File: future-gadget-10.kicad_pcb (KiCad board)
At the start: 2 copper layers, 147.3 x 157.5 mm, 38 parts, among them J1 Conn_02x05_Odd_Even, U1 ProMicro

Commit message: Adds right hand, and updates the connector to be vertical to avoid orientation issues.
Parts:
- added D19: D_Small, Diode_SMD:D_SOD-123, B.Cu at (452.1, 129.5)
- added D20: D_Small, Diode_SMD:D_SOD-123, B.Cu at (431.8, 129.5)
- added D21: D_Small, Diode_SMD:D_SOD-123, B.Cu at (411.5, 119.4)
- added D22: D_Small, Diode_SMD:D_SOD-123, B.Cu at (391.2, 119.4)
- added D23: D_Small, Diode_SMD:D_SOD-123, B.Cu at (370.8, 129.5)
- added D24: D_Small, Diode_SMD:D_SOD-123, B.Cu at (452.1, 149.9)
- added D25: D_Small, Diode_SMD:D_SOD-123, B.Cu at (431.8, 149.9)
- added D26: D_Small, Diode_SMD:D_SOD-123, B.Cu at (411.5, 139.7)
- added D27: D_Small, Diode_SMD:D_SOD-123, B.Cu at (391.2, 139.7)
- added D28: D_Small, Diode_SMD:D_SOD-123, B.Cu at (370.8, 149.9)
- added D29: D_Small, Diode_SMD:D_SOD-123, B.Cu at (452.1, 170.2)
- added D30: D_Small, Diode_SMD:D_SOD-123, B.Cu at (431.8, 170.2)
- added D31: D_Small, Diode_SMD:D_SOD-123, B.Cu at (411.5, 160.0)
- added D32: D_Small, Diode_SMD:D_SOD-123, B.Cu at (391.2, 160.0)
- added D33: D_Small, Diode_SMD:D_SOD-123, B.Cu at (370.8, 170.2)
- added D34: D_Small, Diode_SMD:D_SOD-123, B.Cu at (350.5, 200.7)
- added D35: D_Small, Diode_SMD:D_SOD-123, B.Cu at (345.4, 200.7)
- added D36: D_Small, Diode_SMD:D_SOD-123, B.Cu at (340.4, 200.7)
- added J2: Conn_02x05_Odd_Even, Connector_IDC:IDC-Header_2x05_P2.54mm_Vertical, F.Cu at (340.4, 182.9)
- added MX19: MX-NoLED, MX_Only:MXOnly-1U-Hotswap, F.Cu at (442.0, 137.2)
- added MX20: MX-NoLED, MX_Only:MXOnly-1U-Hotswap, F.Cu at (421.6, 137.2)
- added MX21: MX-NoLED, MX_Only:MXOnly-1U-Hotswap, F.Cu at (401.3, 116.8)
- added MX22: MX-NoLED, MX_Only:MXOnly-1U-Hotswap, F.Cu at (381.0, 116.8)
- added MX23: MX-NoLED, MX_Only:MXOnly-1U-Hotswap, F.Cu at (360.7, 137.2)
- added MX24: MX-NoLED, MX_Only:MXOnly-1U-Hotswap, F.Cu at (442.0, 157.5)
- added MX25: MX-NoLED, MX_Only:MXOnly-1U-Hotswap, F.Cu at (421.6, 157.5)
- added MX26: MX-NoLED, MX_Only:MXOnly-1U-Hotswap, F.Cu at (401.3, 137.2)
- added MX27: MX-NoLED, MX_Only:MXOnly-1U-Hotswap, F.Cu at (381.0, 137.2)
- added MX28: MX-NoLED, MX_Only:MXOnly-1U-Hotswap, F.Cu at (360.7, 157.5)
- added MX29: MX-NoLED, MX_Only:MXOnly-1U-Hotswap, F.Cu at (442.0, 177.8)
- added MX30: MX-NoLED, MX_Only:MXOnly-1U-Hotswap, F.Cu at (421.6, 177.8)
- added MX31: MX-NoLED, MX_Only:MXOnly-1U-Hotswap, F.Cu at (401.3, 157.5)
- added MX32: MX-NoLED, MX_Only:MXOnly-1U-Hotswap, F.Cu at (381.0, 157.5)
- added MX33: MX-NoLED, MX_Only:MXOnly-1U-Hotswap, F.Cu at (360.7, 177.8)
- added MX34: MX-NoLED, MX_Only:MXOnly-1U-Hotswap, F.Cu at (360.7, 208.3)
- added MX35: MX-NoLED, MX_Only:MXOnly-1U-Hotswap, F.Cu at (340.4, 228.6)
- added MX36: MX-NoLED, MX_Only:MXOnly-1U-Hotswap, F.Cu at (320.0, 248.9)
- J1: footprint Connector_IDC:IDC-Header_2x05_P2.54mm_Horizontal -> Connector_IDC:IDC-Header_2x05_P2.54mm_Vertical
- moved J1 6.35 mm to (268.0, 182.9)
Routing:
- net Row4*: track 0.00 -> 171.9 mm, vias 0 -> 4
- net Row5*: track 0.00 -> 158.3 mm, vias 0 -> 5
- net Col9*: track 0.00 -> 142.5 mm
- net Row6*: track 0.00 -> 141.8 mm, vias 0 -> 5
- net Col5*: track 0.00 -> 140.0 mm, vias 0 -> 1
- net Col7*: track 0.00 -> 137.4 mm
- net Col6*: track 0.00 -> 122.4 mm, vias 0 -> 1
- net Col8*: track 0.00 -> 91.6 mm
- net Net-(D36-Pad2): track 0.00 -> 51.3 mm
- net Row7*: track 0.00 -> 24.2 mm
- net Net-(D35-Pad2): track 0.00 -> 20.5 mm
- net Net-(D34-Pad2): track 0.00 -> 17.9 mm
- net Col7: track 48.3 -> 62.3 mm
- net Net-(D27-Pad2): track 0.00 -> 7.77 mm
- net Net-(D26-Pad2): track 0.00 -> 7.77 mm
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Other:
- board size 147.3 x 157.5 mm -> 304.8 x 157.5 mm

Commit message: A little rerouting and a switch of footprints for the MX hotswaps so they render in 3D.
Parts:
- added REF**: Val**, kbd:M2_HOLE, F.Cu at (431.8, 160.0)
- added REF**: Val**, kbd:M2_HOLE, F.Cu at (241.3, 119.4)
- added REF**: Val**, kbd:M2_HOLE, F.Cu at (274.3, 238.8)
- added REF**: Val**, kbd:M2_HOLE, F.Cu at (330.2, 238.8)
- added REF**: Val**, kbd:M2_HOLE, F.Cu at (375.9, 170.2)
- added REF**: Val**, kbd:M2_HOLE, F.Cu at (228.6, 170.2)
- added REF**: Val**, kbd:M2_HOLE, F.Cu at (172.7, 160.0)
- added REF**: Val**, kbd:M2_HOLE, F.Cu at (185.4, 119.4)
- added REF**: Val**, kbd:M2_HOLE, F.Cu at (419.1, 119.4)
- added REF**: Val**, kbd:M2_HOLE, F.Cu at (363.2, 119.4)
- MX1, MX10, MX11, MX12, MX13, MX14, MX15, MX16, MX17, MX18, MX19, MX2, MX20, MX21, MX22, MX23, MX24, MX25, MX26, MX27, MX28, MX29, MX3, MX30, MX31, MX32, MX33, MX34, MX35, MX36, MX4, MX5, MX6, MX7, MX8, MX9: footprint MX_Only:MXOnly-1U-Hotswap -> kbd:CherryMX_Hotswap
- turned MX17 to 315 degrees
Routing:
- net Col8*: track 91.6 -> 159.3 mm
- net Col7*: track 137.4 -> 161.6 mm, vias 0 -> 2
- net Row5*: track 158.3 -> 151.9 mm
- net Col1: track 140.9 -> 137.4 mm
- net Col5*: track 140.0 -> 141.6 mm, vias 1 -> 0
- net Col6*: track 122.4 -> 122.2 mm, vias 1 -> 0

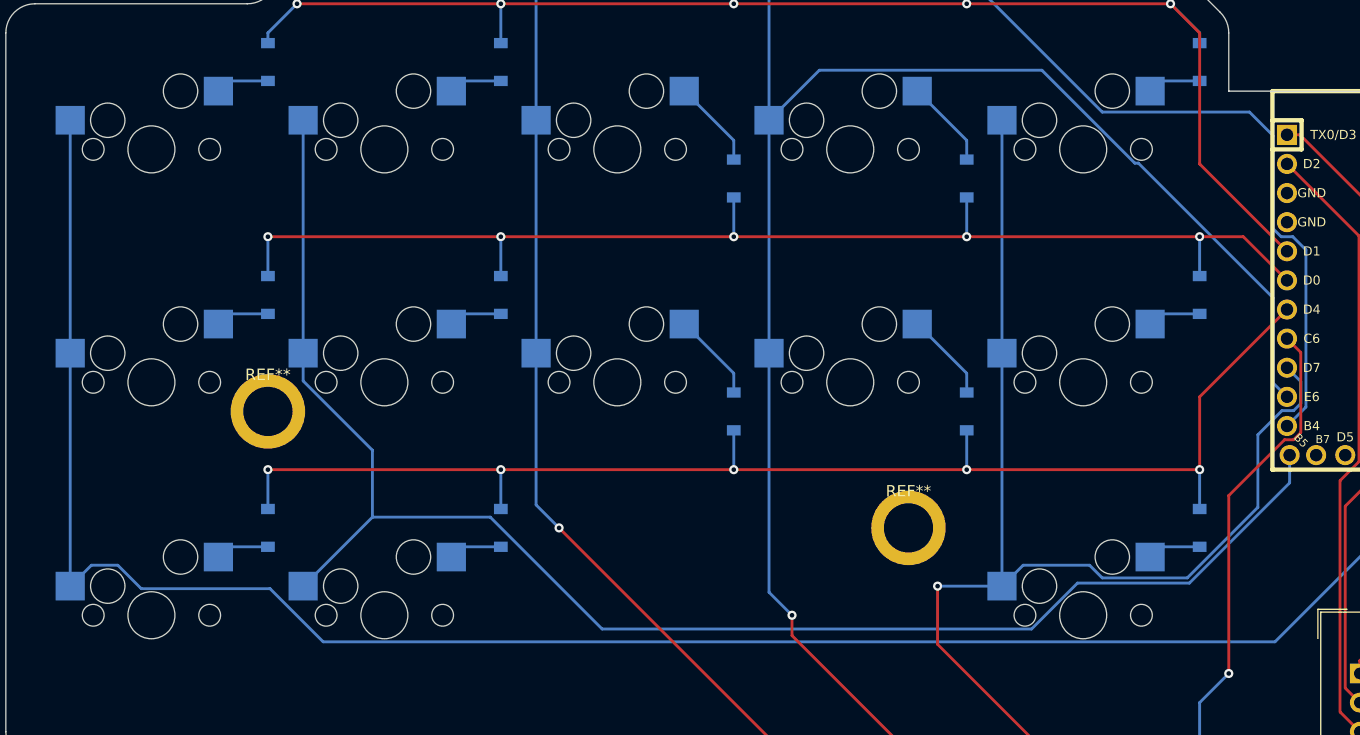
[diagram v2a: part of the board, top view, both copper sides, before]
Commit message: Rerouted some tracks to avoid proximity issues.
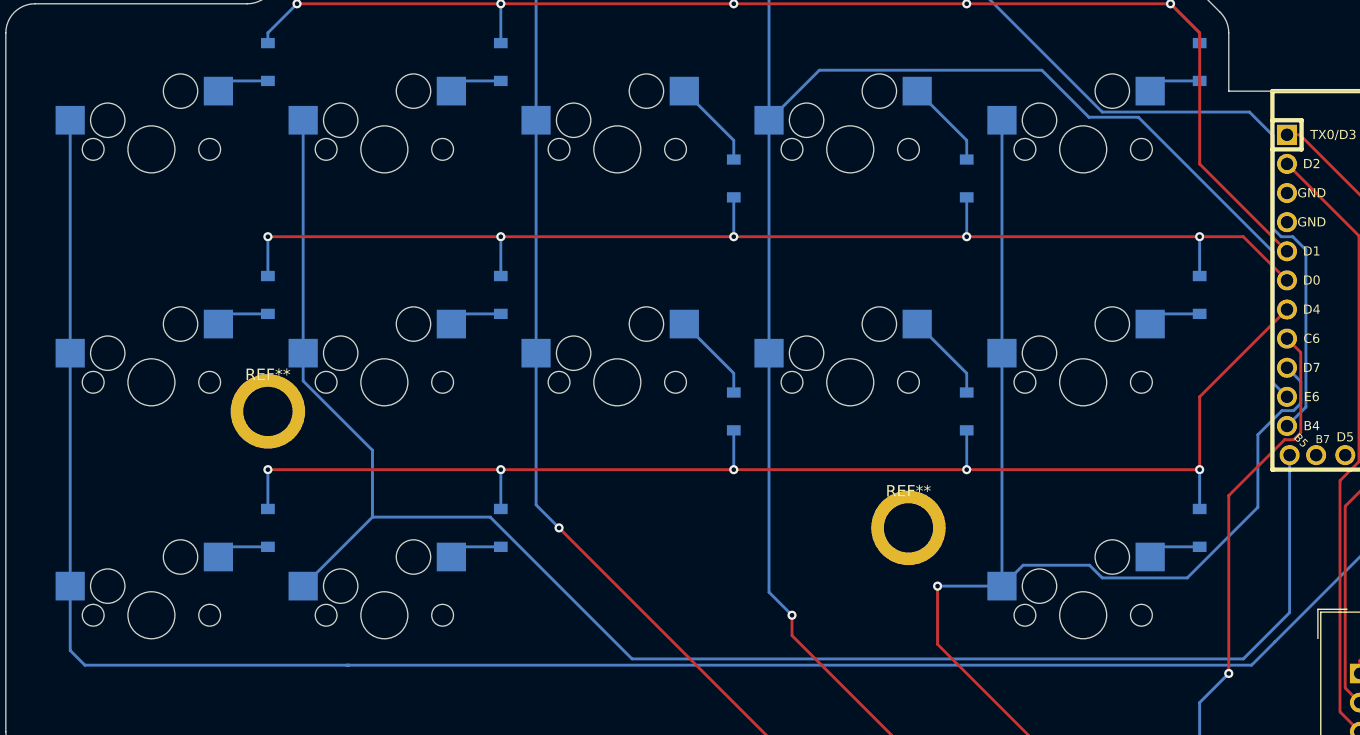
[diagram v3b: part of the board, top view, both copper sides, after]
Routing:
- net Col1: track 137.4 -> 146.2 mm
- net Col0: track 172.3 -> 176.0 mm
- net Col3: track 190.0 -> 192.4 mm
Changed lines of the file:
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@@
     (thickness 1.6)
     (drawings 62)
-    (tracks 409)
+    (tracks 407)
     (zones 0)
     (modules 85)
@@
   (segment (start 155.475 154.94) (end 155.475 175.26) (width 0.25) (layer B.Cu) (net 12) (status 30))
   (segment (start 260.571099 180.118901) (end 276.86 163.83) (width 0.25) (layer B.Cu) (net 12) (status 20))
-  (segment (start 172.906097 175.481099) (end 177.543899 180.118901) (width 0.25) (layer B.Cu) (net 12))
-  (segment (start 177.543899 180.118901) (end 260.571099 180.118901) (width 0.25) (layer B.Cu) (net 12))
-  (segment (start 159.626001 173.434999) (end 161.672101 175.481099) (width 0.25) (layer B.Cu) (net 12))
-  (segment (start 161.672101 175.481099) (end 172.906097 175.481099) (width 0.25) (layer B.Cu) (net 12))
-  (segment (start 157.325001 173.434999) (end 159.626001 173.434999) (width 0.25) (layer B.Cu) (net 12))
-  (segment (start 155.5 175.26) (end 157.325001 173.434999) (width 0.25) (layer B.Cu) (net 12) (status 10))
   (segment (start 155.475 175.26) (end 155.5 175.26) (width 0.25) (layer B.Cu) (net 12) (status 30))
+  (segment (start 258.535001 182.154999) (end 260.571099 180.118901) (width 0.25) (layer B.Cu) (net 12))
+  (segment (start 155.475 175.26) (end 155.475 180.875) (width 0.25) (layer B.Cu) (net 12))
+  (segment (start 156.754999 182.154999) (end 179.795001 182.154999) (width 0.25) (layer B.Cu) (net 12))
+  (segment (start 155.475 180.875) (end 156.754999 182.154999) (width 0.25) (layer B.Cu) (net 12))
+  (segment (start 179.795001 182.154999) (end 258.535001 182.154999) (width 0.25) (layer B.Cu) (net 12))
+  (segment (start 179.579997 182.154999) (end 179.795001 182.154999) (width 0.25) (layer B.Cu) (net 12))
   (segment (start 175.795 134.62) (end 175.795 154.94) (width 0.25) (layer B.Cu) (net 13) (status 30))
-  (segment (start 239.336001 179.000001) (end 243.340992 174.99501) (width 0.25) (layer B.Cu) (net 13))
-  (segment (start 201.874999 179.000001) (end 239.336001 179.000001) (width 0.25) (layer B.Cu) (net 13))
-  (segment (start 192.114999 169.240001) (end 201.874999 179.000001) (width 0.25) (layer B.Cu) (net 13))
-  (segment (start 261.8486 166.252812) (end 261.8486 163.83) (width 0.25) (layer B.Cu) (net 13) (status 20))
-  (segment (start 243.340992 174.99501) (end 253.106402 174.99501) (width 0.25) (layer B.Cu) (net 13))
-  (segment (start 181.839999 169.240001) (end 192.114999 169.240001) (width 0.25) (layer B.Cu) (net 13))
   (segment (start 175.82 175.26) (end 181.839999 169.240001) (width 0.25) (layer B.Cu) (net 13) (status 10))
-  (segment (start 253.106402 174.99501) (end 261.8486 166.252812) (width 0.25) (layer B.Cu) (net 13))
   (segment (start 175.795 175.26) (end 175.82 175.26) (width 0.25) (layer B.Cu) (net 13) (status 30))
   (segment (start 175.795 157.362002) (end 181.839999 163.407001) (width 0.25) (layer B.Cu) (net 13))
   (segment (start 181.839999 163.407001) (end 181.839999 169.240001) (width 0.25) (layer B.Cu) (net 13))
   (segment (start 175.795 154.94) (end 175.795 157.362002) (width 0.25) (layer B.Cu) (net 13) (status 10))
+  (segment (start 192.114999 169.240001) (end 181.839999 169.240001) (width 0.25) (layer B.Cu) (net 13))
+  (segment (start 204.484998 181.61) (end 192.114999 169.240001) (width 0.25) (layer B.Cu) (net 13))
+  (segment (start 257.81 181.61) (end 204.484998 181.61) (width 0.25) (layer B.Cu) (net 13))
+  (segment (start 261.8486 177.5714) (end 257.81 181.61) (width 0.25) (layer B.Cu) (net 13))
+  (segment (start 261.8486 163.83) (end 261.8486 177.5714) (width 0.25) (layer B.Cu) (net 13))
   (segment (start 250.572 131.19) (end 249.682 132.08) (width 0.25) (layer B.Cu) (net 14) (status 30))
   (segment (start 254 131.19) (end 250.572 131.19) (width 0.25) (layer B.Cu) (net 14) (status 30))
@@
   (segment (start 216.435 114.3) (end 216.435 134.62) (width 0.25) (layer B.Cu) (net 27) (status 30))
   (segment (start 216.435 134.62) (end 216.435 154.94) (width 0.25) (layer B.Cu) (net 27) (status 30))
-  (segment (start 248.653003 138.360001) (end 260.418699 150.125697) (width 0.25) (layer B.Cu) (net 27))
-  (segment (start 260.418699 157.548699) (end 261.62 158.75) (width 0.25) (layer B.Cu) (net 27) (status 20))
-  (segment (start 240.238997 130.254999) (end 248.343999 138.360001) (width 0.25) (layer B.Cu) (net 27))
-  (segment (start 220.825001 130.254999) (end 240.238997 130.254999) (width 0.25) (layer B.Cu) (net 27))
-  (segment (start 260.418699 150.125697) (end 260.418699 157.548699) (width 0.25) (layer B.Cu) (net 27))
-  (segment (start 216.46 134.62) (end 220.825001 130.254999) (width 0.25) (layer B.Cu) (net 27) (status 10))
-  (segment (start 248.343999 138.360001) (end 248.653003 138.360001) (width 0.25) (layer B.Cu) (net 27))
-  (segment (start 216.435 134.62) (end 216.46 134.62) (width 0.25) (layer B.Cu) (net 27) (status 30))
   (via (at 218.44 177.8) (size 0.8) (drill 0.4) (layers F.Cu B.Cu) (net 27))
   (segment (start 216.435 175.795) (end 218.44 177.8) (width 0.25) (layer B.Cu) (net 27))
@@
   (segment (start 218.44 177.8) (end 218.44 179.576002) (width 0.25) (layer F.Cu) (net 27))
   (segment (start 259.08 218.44) (end 261.945919 221.305919) (width 0.25) (layer B.Cu) (net 27) (status 20))
+  (segment (start 260.418699 157.548699) (end 261.62 158.75) (width 0.25) (layer B.Cu) (net 27))
+  (segment (start 244.339009 134.355011) (end 248.655011 134.355011) (width 0.25) (layer B.Cu) (net 27))
+  (segment (start 216.46 134.62) (end 220.825001 130.254999) (width 0.25) (layer B.Cu) (net 27))
+  (segment (start 240.238997 130.254999) (end 244.339009 134.355011) (width 0.25) (layer B.Cu) (net 27))
+  (segment (start 260.418699 146.118699) (end 260.418699 157.548699) (width 0.25) (layer B.Cu) (net 27))
+  (segment (start 220.825001 130.254999) (end 240.238997 130.254999) (width 0.25) (layer B.Cu) (net 27))
+  (segment (start 248.655011 134.355011) (end 260.418699 146.118699) (width 0.25) (layer B.Cu) (net 27))
+  (segment (start 216.435 134.62) (end 216.46 134.62) (width 0.25) (layer B.Cu) (net 27))
   (segment (start 236.755 134.62) (end 236.755 154.94) (width 0.25) (layer B.Cu) (net 28) (status 30))
   (segment (start 236.755 154.94) (end 236.755 175.26) (width 0.25) (layer B.Cu) (net 28) (status 30))

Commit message: A little more rerouting to avoid tracks near solder points.
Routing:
- net Row5*: track 151.9 -> 160.3 mm
- net Col1: track 146.2 -> 152.3 mm
- net Col6*: track 122.2 -> 126.5 mm
- net Col3: track 192.4 -> 196.6 mm
- net Col8*: track 159.3 -> 161.6 mm, vias 0 -> 1
